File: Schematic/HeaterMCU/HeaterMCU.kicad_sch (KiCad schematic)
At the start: 57 parts, among them J301 To µTracer, J302 Firmware, J303 To PSU Board, Q301 BSS138, Q302 BSS138, SW301 RESET, U301 TPS54302, U302 ATMEGA328P-AU, U303 INA219AIDCNR, U304 Display_IPS_1.3_SPI, Y301 8MHz

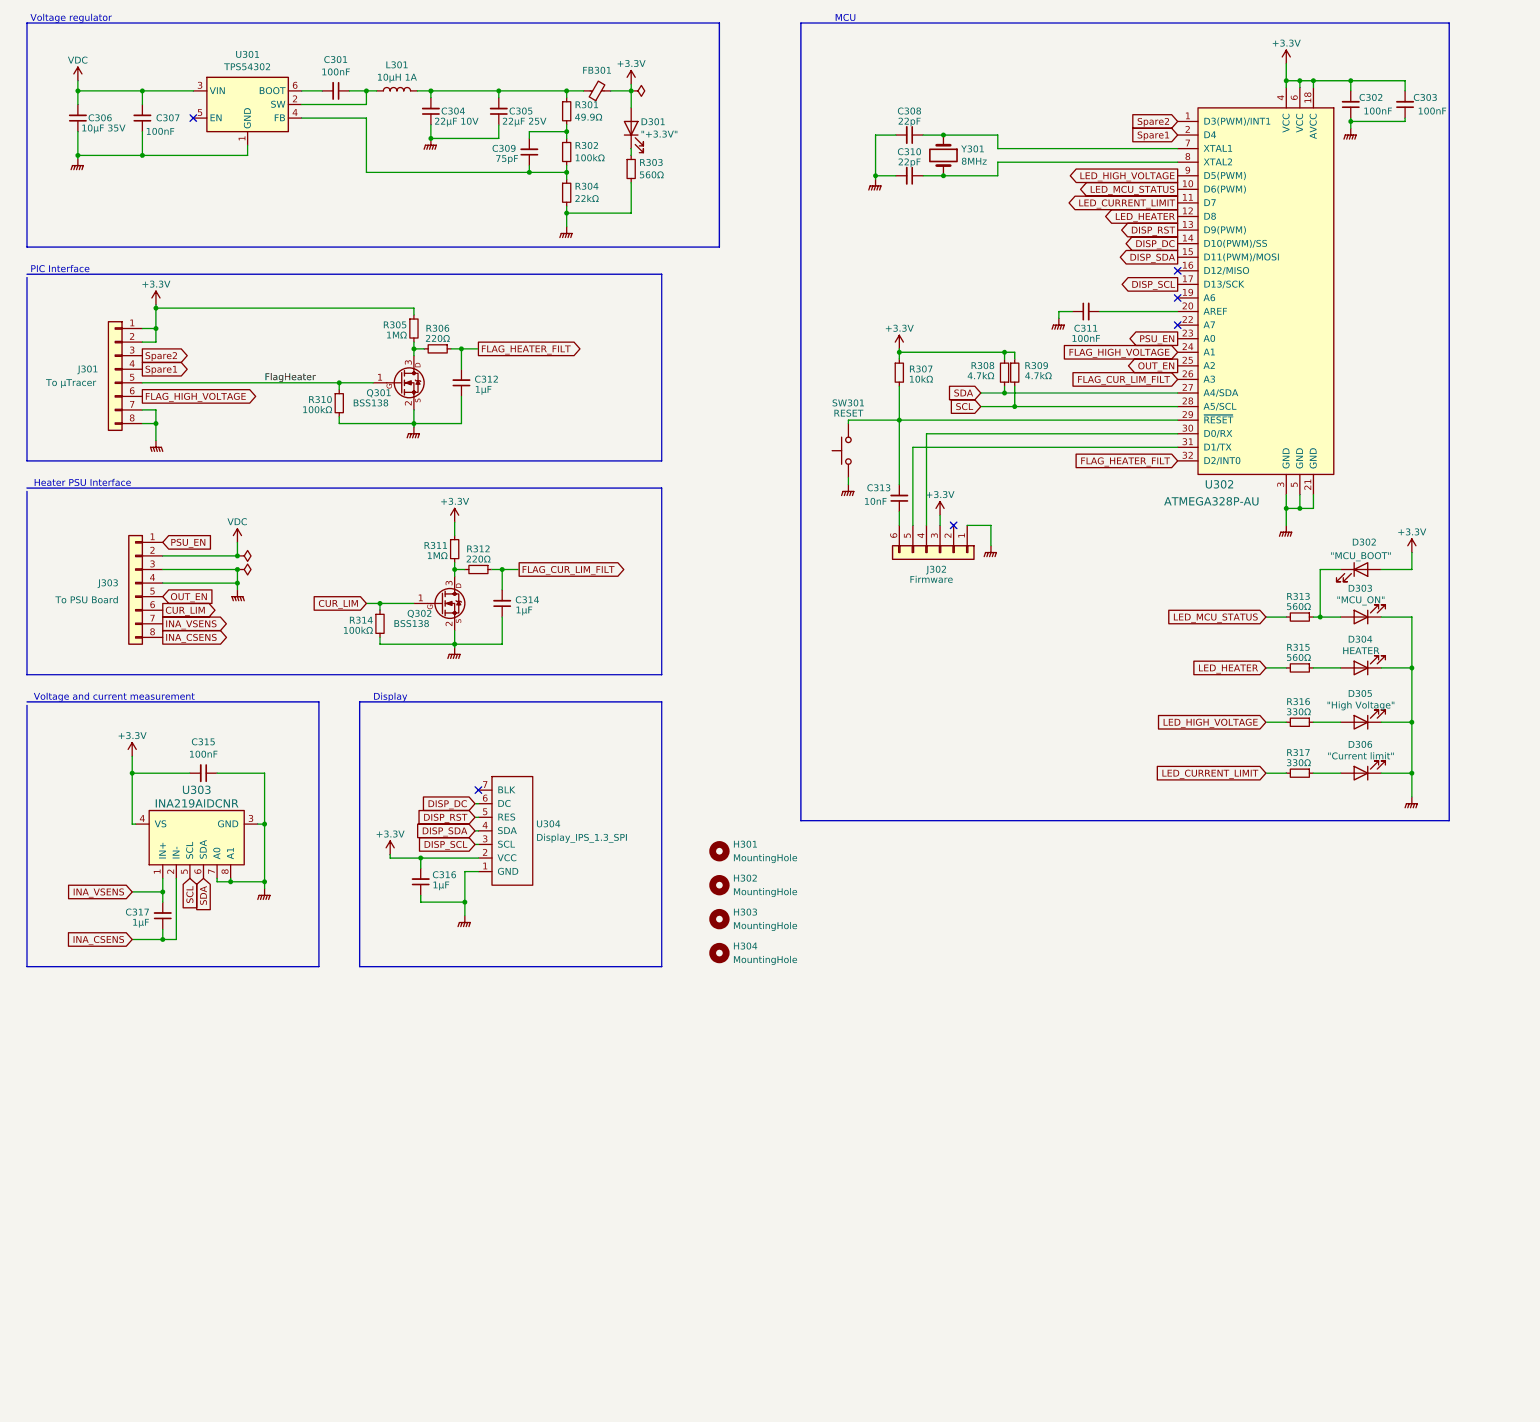
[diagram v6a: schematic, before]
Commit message: New status LED layout
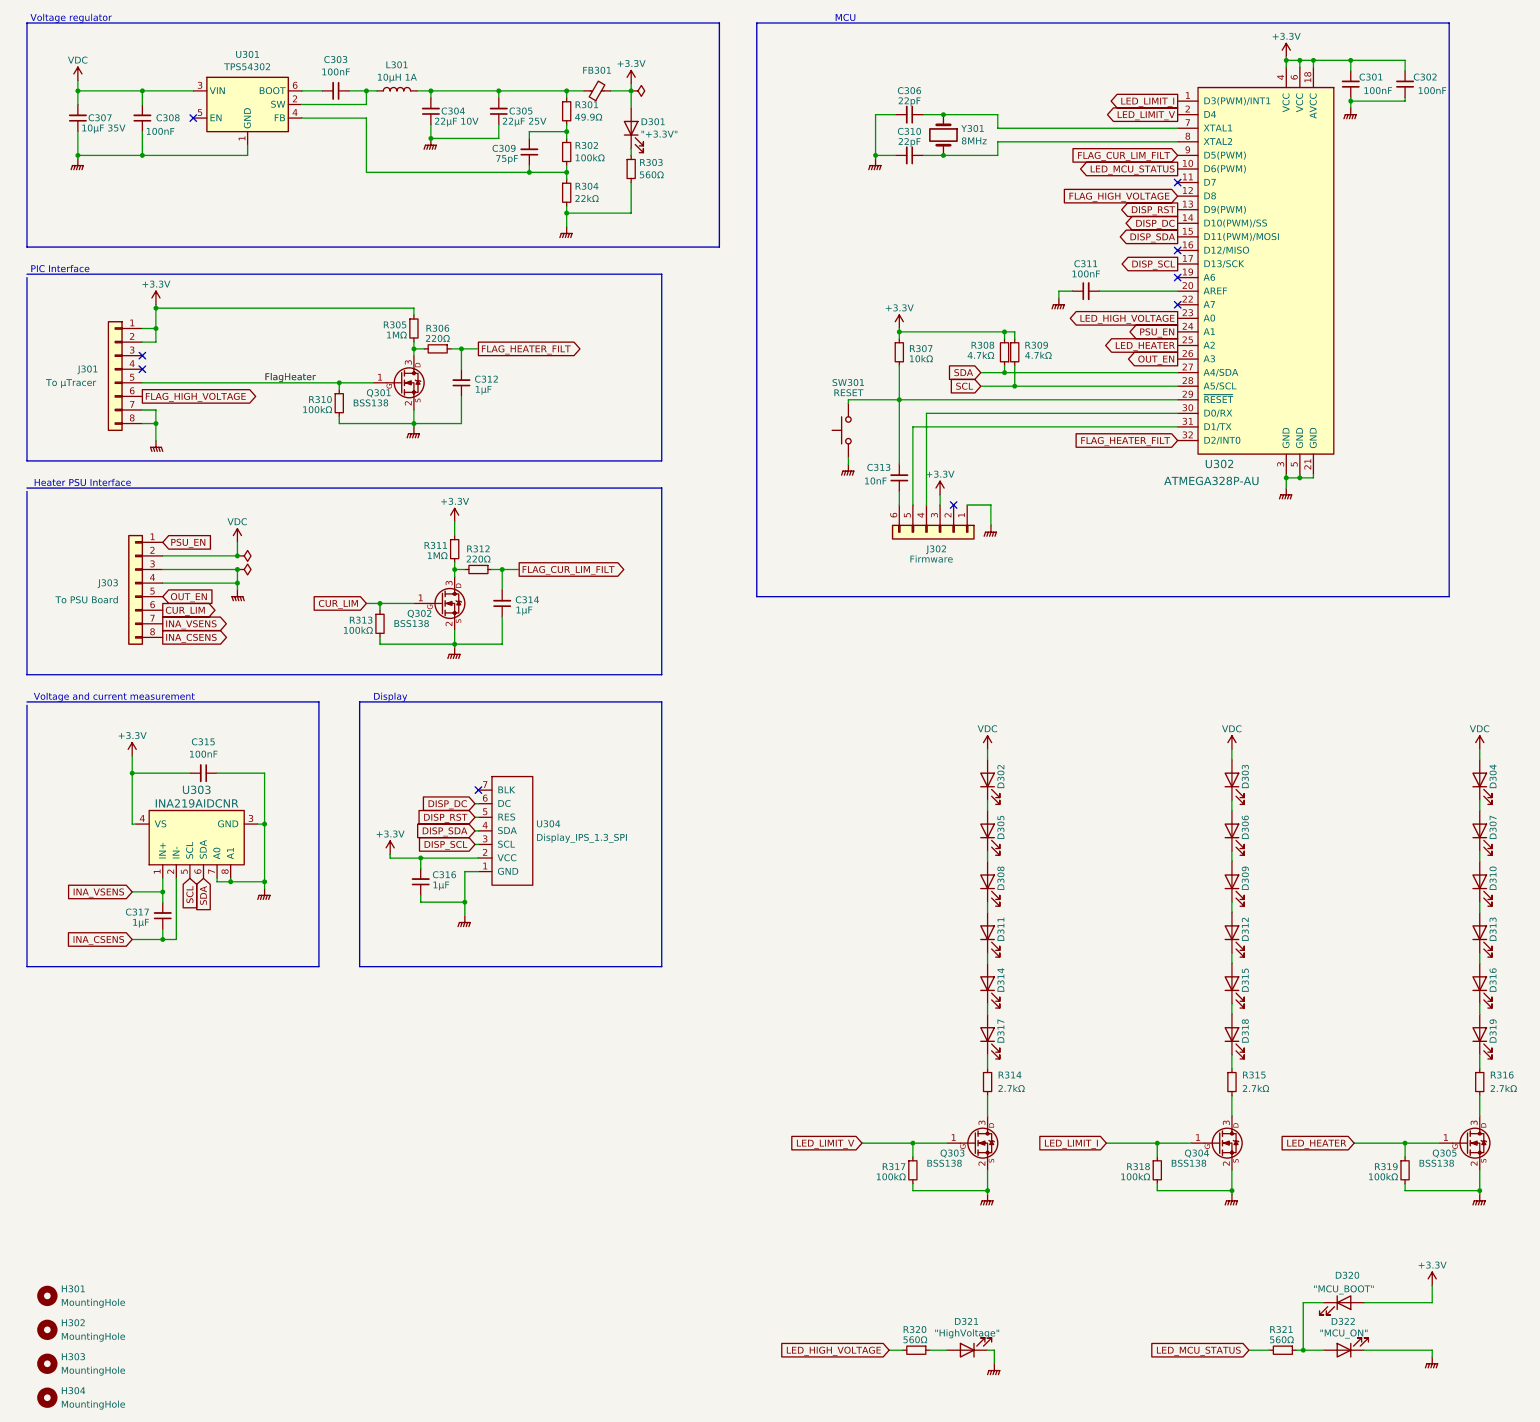
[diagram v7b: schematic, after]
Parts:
- added D302, D308, D311, D314, D317: "Voltage limit", LED_SMD:LED_0603_1608Metric_Pad1.05x0.95mm_HandSolder, symbol Device:LED
- added D303, D309, D312, D315, D318: "Current limit", LED_SMD:LED_0603_1608Metric_Pad1.05x0.95mm_HandSolder, symbol Device:LED
- added D307, D310, D313, D316, D319: "Heater", LED_SMD:LED_0603_1608Metric_Pad1.05x0.95mm_HandSolder, symbol Device:LED
- added D321: "HighVoltage", LED_SMD:LED_0603_1608Metric_Pad1.05x0.95mm_HandSolder, symbol Device:LED
- added Q303, Q304, Q305: BSS138, Package_TO_SOT_SMD:SOT-23, symbol myDevices:BSS138
- added R317, R318, R319: 100kΩ, Resistor_SMD:R_0603_1608Metric_Pad0.98x0.95mm_HandSolder, symbol Device:R_Small
- added R320: 560Ω, Resistor_SMD:R_0603_1608Metric_Pad0.98x0.95mm_HandSolder, symbol Device:R_Small
- D304: value HEATER -> "Heater"
- D305: value "High Voltage" -> "Voltage limit"
- R314: renamed from R317; value 330Ω -> 2.7kΩ
- R315: value 560Ω -> 2.7kΩ
- R316: value 330Ω -> 2.7kΩ
- renumbered C302 to C301, C303 to C302, C301 to C303, C308 to C306, C306 to C307, C307 to C308, D302 to D320, D303 to D322, R314 to R313, R313 to R321
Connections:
- net FLAG_CUR_LIM_FILT: now also U302.9 (D5(PWM)); no longer U302.26 (A3)
- net FLAG_HIGH_VOLTAGE: now also U302.12 (D8); no longer U302.24 (A1)
- net GNDPWR: now also D321.1 (K), Q303.2 (S), Q304.2 (S), Q305.2 (S), R317.2, R318.2, R319.2; no longer D304.1 (K), D305.1 (K), D306.1 (K)
- net LED_HEATER: now also U302.25 (A2), Q305.1 (G), R319.1; no longer R315.2, U302.12 (D8)
- net LED_HIGH_VOLTAGE: now also U302.23 (A0), R320.2; no longer R316.2, U302.9 (D5(PWM))
- net OUT_EN: now also U302.26 (A3); no longer U302.25 (A2)
- net PSU_EN: now also U302.24 (A1); no longer U302.23 (A0)
- net VDC: now also D304.2 (A), D302.2 (A), D303.2 (A)
- net at R315.1: now also D318.1 (K); no longer D304.2 (A)
- net at D305.2 (A): now also D302.1 (K); no longer R316.1
- net at D306.2 (A): now also D303.1 (K); no longer R314.1
- net LED_CURRENT_LIMIT: no longer names the net of U302.11 (D7)
- net LED_CURRENT_LIMIT: no longer R314.2
- net Spare1: no longer names the net of J301.4 (Pin_4)
- net Spare1: no longer U302.2 (D4)
- net Spare2: no longer names the net of J301.3 (Pin_3)
- net Spare2: no longer U302.1 (D3(PWM)/INT1)
- new net: D307.1 (K), D310.2 (A)
- new net: D304.1 (K), D307.2 (A)
- new net: D314.1 (K), D317.2 (A)
- new net: D311.1 (K), D314.2 (A)
- new net: D315.1 (K), D318.2 (A)
- new net: D312.1 (K), D315.2 (A)
- new net: D305.1 (K), D308.2 (A)
- new net: D316.1 (K), D319.2 (A)
- new net: D313.1 (K), D316.2 (A)
- new net: D319.1 (K), R316.1
- new net: D308.1 (K), D311.2 (A)
- new net: Q303.3 (D), R314.2
- new net: D306.1 (K), D309.2 (A)
- new net: D317.1 (K), R314.1
- new net: Q304.3 (D), R315.2
- new net: D321.2 (A), R320.1
- new net: Q305.3 (D), R316.2
- new net: D309.1 (K), D312.2 (A)
- new net: D310.1 (K), D313.2 (A)
- new net LED_LIMIT_I: Q304.1 (G), R318.1, U302.1 (D3(PWM)/INT1)
- new net LED_LIMIT_V: Q303.1 (G), R317.1, U302.2 (D4)
- no-connect marks 6 -> 9
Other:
- moved on the sheet: C301, C302, C306, C310, C311, C313, D320, D322, H301, H302, H303, H304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

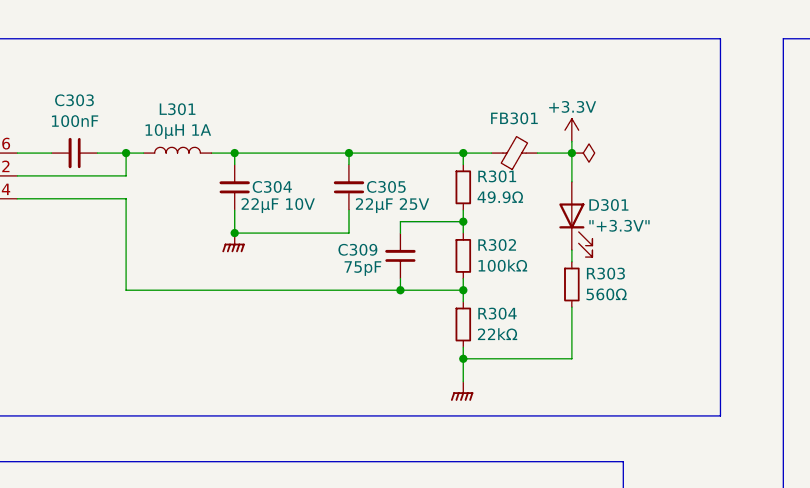
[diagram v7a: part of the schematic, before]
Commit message: Updated component values
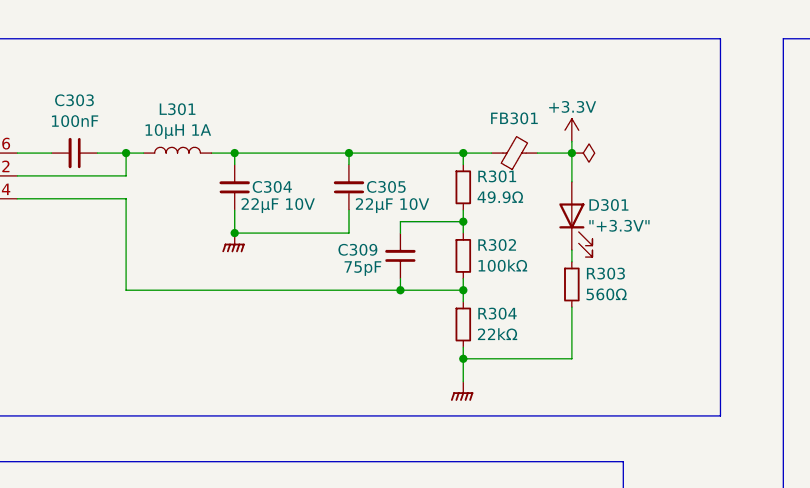
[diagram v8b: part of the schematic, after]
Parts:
- C305: value 22µF 25V -> 22µF 10V
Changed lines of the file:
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@@
       (effects (font (size 1.27 1.27)) (justify right))
     )
-    (property "Value" "22µF 25V" (id 1) (at 104.775 33.655 0)
+    (property "Value" "22µF 10V" (id 1) (at 104.775 33.655 0)
       (effects (font (size 1.27 1.27)) (justify right))
     )
@@
     )
     (path "/a8b43ed0-8229-48ba-a25d-209c06b961d3"
-      (reference "C305") (unit 1) (value "22µF 25V") (footprint "Capacitor_SMD:C_0603_1608Metric_Pad1.08x0.95mm_HandSolder")
+      (reference "C305") (unit 1) (value "22µF 10V") (footprint "Capacitor_SMD:C_0603_1608Metric_Pad1.08x0.95mm_HandSolder")
     )
     (path "/73f77089-2eb9-466d-9b6b-43d457e33e64"
